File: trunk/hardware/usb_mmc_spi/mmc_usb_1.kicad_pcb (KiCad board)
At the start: 2 copper layers, 47.6 x 27.3 mm, 25 parts, among them J301 MINI-USB-5P-3400020P1, K301 CONN_3, P301 CONN_5X2, P302 MICRO-SDCARD-CONNECTOR-330006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, P303 CONN_10X2, P304 CONN_10X2, P305 CONN_1, P306 CONN_1, U301 FT232RL

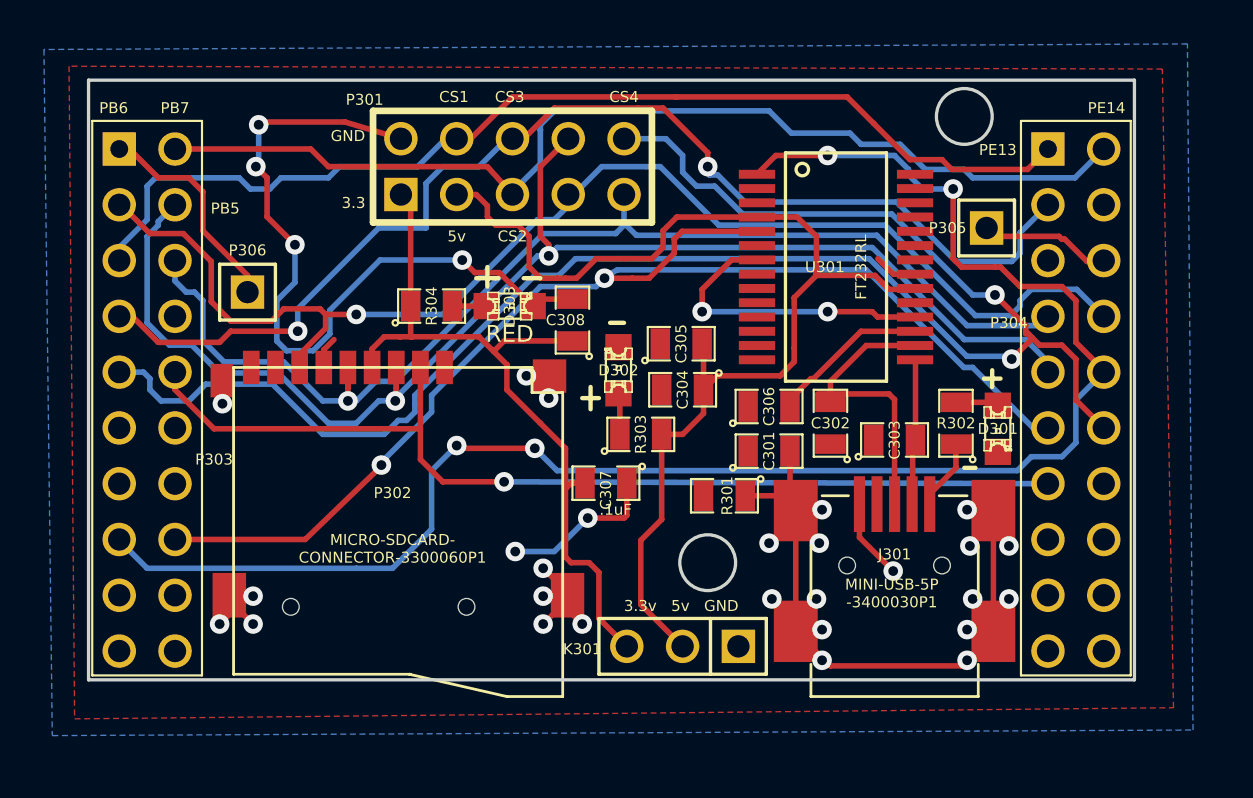
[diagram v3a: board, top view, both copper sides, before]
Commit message: better naming
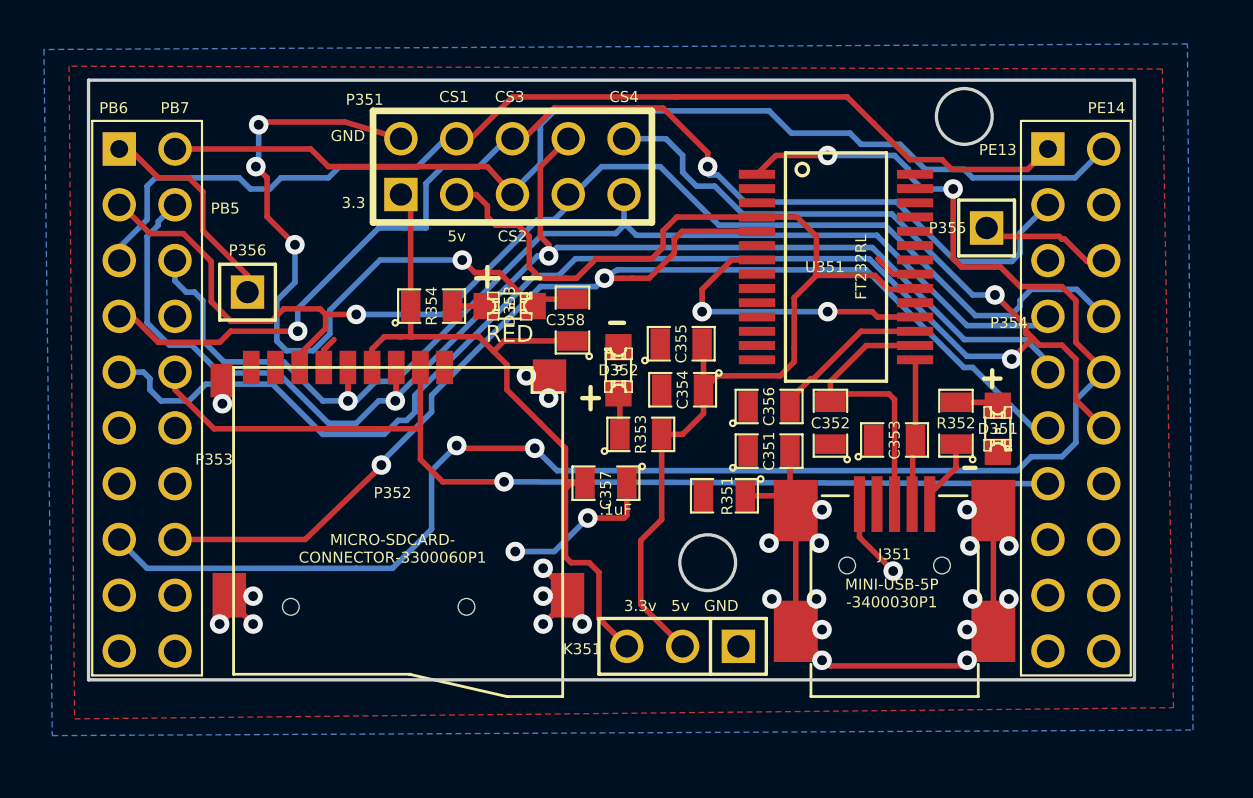
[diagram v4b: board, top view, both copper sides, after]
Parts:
- renumbered C301 to C351, C302 to C352, C303 to C353, C304 to C354, C305 to C355, C306 to C356, C307 to C357, C308 to C358, D301 to D351, D302 to D352, D303 to D353, J301 to J351, K301 to K351, P301 to P351, P302 to P352, P303 to P353, P304 to P354, P305 to P355, P306 to P356, R301 to R351, R302 to R352, R303 to R353, R304 to R354, U301 to U351
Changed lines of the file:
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@@
     (tags "MICRO SD MEMORY CARD MMC")
     (attr smd)
-    (fp_text reference P302 (at -1.778 0.254 360) (layer F.SilkS)
+    (fp_text reference P352 (at -1.778 0.254 360) (layer F.SilkS)
       (effects (font (size 0.50038 0.50038) (thickness 0.1016)))
     )
@@
       (layers F.Cu F.Paste F.Mask)
     )
-    (pad G301 smd rect (at -6.893 8.032 270) (size 1.524 1.016)
+    (pad G351 smd rect (at -6.893 8.032 270) (size 1.524 1.016)
       (layers F.Cu F.Paste F.Mask)
       (net 13 GND)
@@
     (at 207.391 168.656)
     (attr smd)
-    (fp_text reference C301 (at 0 0 90) (layer F.SilkS)
+    (fp_text reference C351 (at 0 0 90) (layer F.SilkS)
       (effects (font (size 0.50038 0.50038) (thickness 0.1016)))
     )
@@
     (at 210.185 167.386 90)
     (attr smd)
-    (fp_text reference C302 (at 0 0 180) (layer F.SilkS)
+    (fp_text reference C352 (at 0 0 180) (layer F.SilkS)
       (effects (font (size 0.50038 0.50038) (thickness 0.1016)))
     )
@@
     (at 213.106 168.148)
     (attr smd)
-    (fp_text reference C303 (at 0 0 90) (layer F.SilkS)
+    (fp_text reference C353 (at 0 0 90) (layer F.SilkS)
       (effects (font (size 0.50038 0.50038) (thickness 0.1016)))
     )
@@
     (at 203.454 165.862 180)
     (attr smd)
-    (fp_text reference C304 (at 0 0 270) (layer F.SilkS)
+    (fp_text reference C354 (at 0 0 270) (layer F.SilkS)
       (effects (font (size 0.50038 0.50038) (thickness 0.1016)))
     )
@@
     (at 203.3905 163.7665)
     (attr smd)
-    (fp_text reference C305 (at 0 0 90) (layer F.SilkS)
+    (fp_text reference C355 (at 0 0 90) (layer F.SilkS)
       (effects (font (size 0.50038 0.50038) (thickness 0.1016)))
     )
@@
     (at 207.391 166.624)
     (attr smd)
-    (fp_text reference C306 (at 0 0 90) (layer F.SilkS)
+    (fp_text reference C356 (at 0 0 90) (layer F.SilkS)
       (effects (font (size 0.50038 0.50038) (thickness 0.1016)))
     )
@@
     (tags "LED 0805 SMD")
     (attr smd)
-    (fp_text reference D301 (at 0 0 360) (layer F.SilkS)
+    (fp_text reference D351 (at 0 0 360) (layer F.SilkS)
       (effects (font (size 0.50038 0.50038) (thickness 0.1016)))
     )
@@
     (tags "LED 0805 SMD")
     (attr smd)
-    (fp_text reference D302 (at 0 0 180) (layer F.SilkS)
+    (fp_text reference D352 (at 0 0 180) (layer F.SilkS)
       (effects (font (size 0.50038 0.50038) (thickness 0.1016)))
     )
@@
     (at 205.359 170.688 180)
     (attr smd)
-    (fp_text reference R301 (at -0.127 0 270) (layer F.SilkS)
+    (fp_text reference R351 (at -0.127 0 270) (layer F.SilkS)
       (effects (font (size 0.50038 0.50038) (thickness 0.1016)))
     )
@@
     (at 215.9 167.386 90)
     (attr smd)
-    (fp_text reference R302 (at 0 0 180) (layer F.SilkS)
+    (fp_text reference R352 (at 0 0 180) (layer F.SilkS)
       (effects (font (size 0.50038 0.50038) (thickness 0.1016)))
     )
@@
     (at 201.549 167.894)
     (attr smd)
-    (fp_text reference R303 (at 0 0 90) (layer F.SilkS)
+    (fp_text reference R353 (at 0 0 90) (layer F.SilkS)
       (effects (font (size 0.50038 0.50038) (thickness 0.1016)))
     )
@@
     (at 210.439 160.274 270)
     (descr SSOP-16)
-    (fp_text reference U301 (at 0 0.508 360) (layer F.SilkS)
+    (fp_text reference U351 (at 0 0.508 360) (layer F.SilkS)
       (effects (font (size 0.50038 0.50038) (thickness 0.1016)))
     )
@@
     (tags "LED 0805 SMD")
     (attr smd)
-    (fp_text reference D303 (at 0 0 90) (layer F.SilkS)
+    (fp_text reference D353 (at 0 0 90) (layer F.SilkS)
       (effects (font (size 0.50038 0.50038) (thickness 0.1016)))
     )
@@
     (at 192.024 162.052)
     (attr smd)
-    (fp_text reference R304 (at 0 0 90) (layer F.SilkS)
+    (fp_text reference R354 (at 0 0 90) (layer F.SilkS)
       (effects (font (size 0.50038 0.50038) (thickness 0.1016)))
     )
@@
     (descr "Connecter 3 pins")
     (tags "PIN 3")
-    (fp_text reference K301 (at 4.572 -0.127 180) (layer F.SilkS)
+    (fp_text reference K351 (at 4.572 -0.127 180) (layer F.SilkS)
       (effects (font (size 0.50038 0.50038) (thickness 0.1016)))
     )
@@
   (module PIN_ARRAY_10X2 (layer F.Cu)
     (at 179.07 166.37 270)
-    (fp_text reference P303 (at 2.667 -3.048 360) (layer F.SilkS)
+    (fp_text reference P353 (at 2.667 -3.048 360) (layer F.SilkS)
       (effects (font (size 0.50038 0.50038) (thickness 0.1016)))
     )
@@
   (module PIN_ARRAY_10X2 (layer F.Cu)
     (at 221.361 166.37 270)
-    (fp_text reference P304 (at -3.556 3.048 360) (layer F.SilkS)
+    (fp_text reference P354 (at -3.556 3.048 360) (layer F.SilkS)
       (effects (font (size 0.50038 0.50038) (thickness 0.1016)))
     )
@@
     (tags "USB MINI 5 SMD-1")
     (attr smd)
-    (fp_text reference J301 (at 0 -1.905) (layer F.SilkS)
+    (fp_text reference J351 (at 0 -1.905) (layer F.SilkS)
       (effects (font (size 0.50038 0.50038) (thickness 0.1016)))
     )
@@
     (descr "1 pin")
     (tags "CONN DEV")
-    (fp_text reference P305 (at -1.778 0) (layer F.SilkS)
+    (fp_text reference P355 (at -1.778 0) (layer F.SilkS)
       (effects (font (size 0.50038 0.50038) (thickness 0.1016)))
     )
@@
     (descr "Double rangee de contacts 2 x 5 pins")
     (tags CONN)
-    (fp_text reference P301 (at -6.731 -3.048) (layer F.SilkS)
+    (fp_text reference P351 (at -6.731 -3.048) (layer F.SilkS)
       (effects (font (size 0.50038 0.50038) (thickness 0.1016)))
     )
@@
     (descr "1 pin")
     (tags "CONN DEV")
-    (fp_text reference P306 (at 0 -1.905) (layer F.SilkS)
+    (fp_text reference P356 (at 0 -1.905) (layer F.SilkS)
       (effects (font (size 0.50038 0.50038) (thickness 0.1016)))
     )
@@
     (at 199.9615 170.1165 180)
     (attr smd)
-    (fp_text reference C307 (at 0 -0.3175 270) (layer F.SilkS)
+    (fp_text reference C357 (at 0 -0.3175 270) (layer F.SilkS)
       (effects (font (size 0.50038 0.50038) (thickness 0.10922)))
     )
@@
     (at 198.4375 162.687 90)
     (attr smd)
-    (fp_text reference C308 (at 0 -0.3175 180) (layer F.SilkS)
+    (fp_text reference C358 (at 0 -0.3175 180) (layer F.SilkS)
       (effects (font (size 0.50038 0.50038) (thickness 0.10922)))
     )

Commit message: CAN_TX net
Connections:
- net N-0000033 renamed /CAN_TX

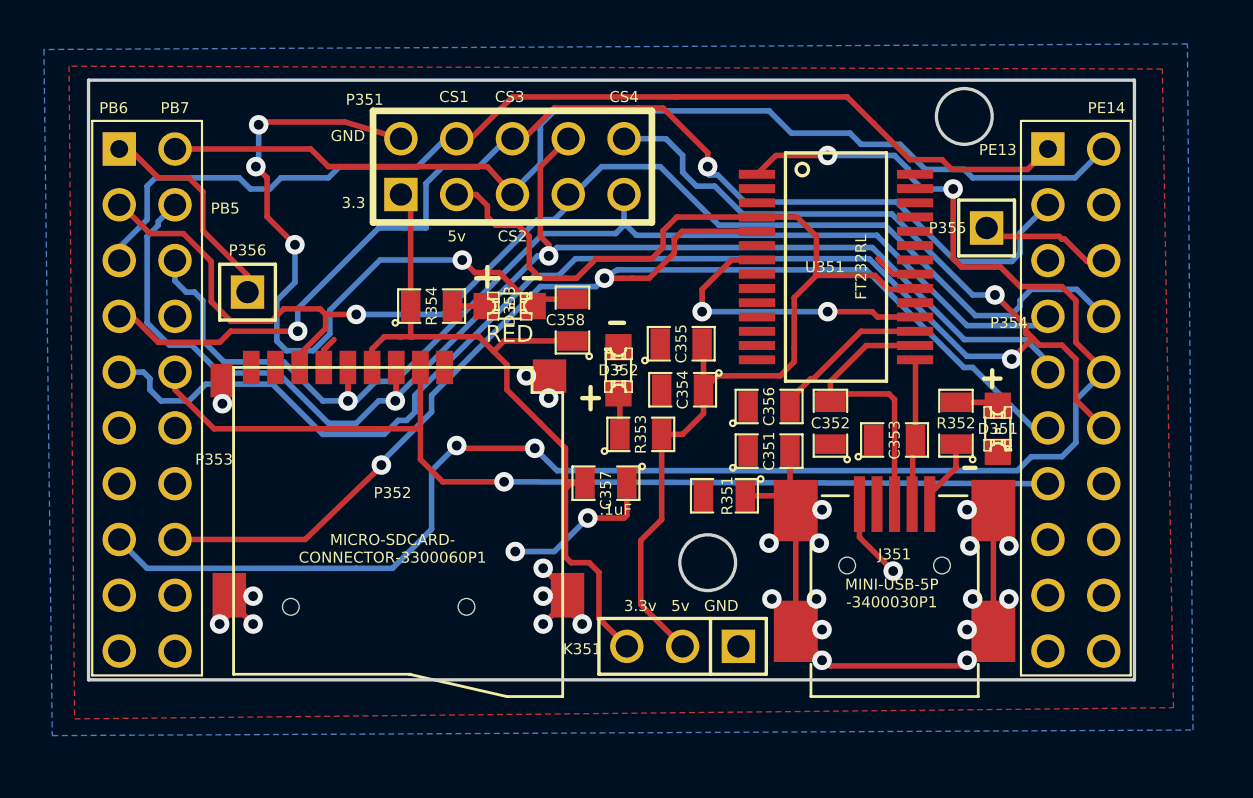
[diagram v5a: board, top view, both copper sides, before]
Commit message: some track improvements
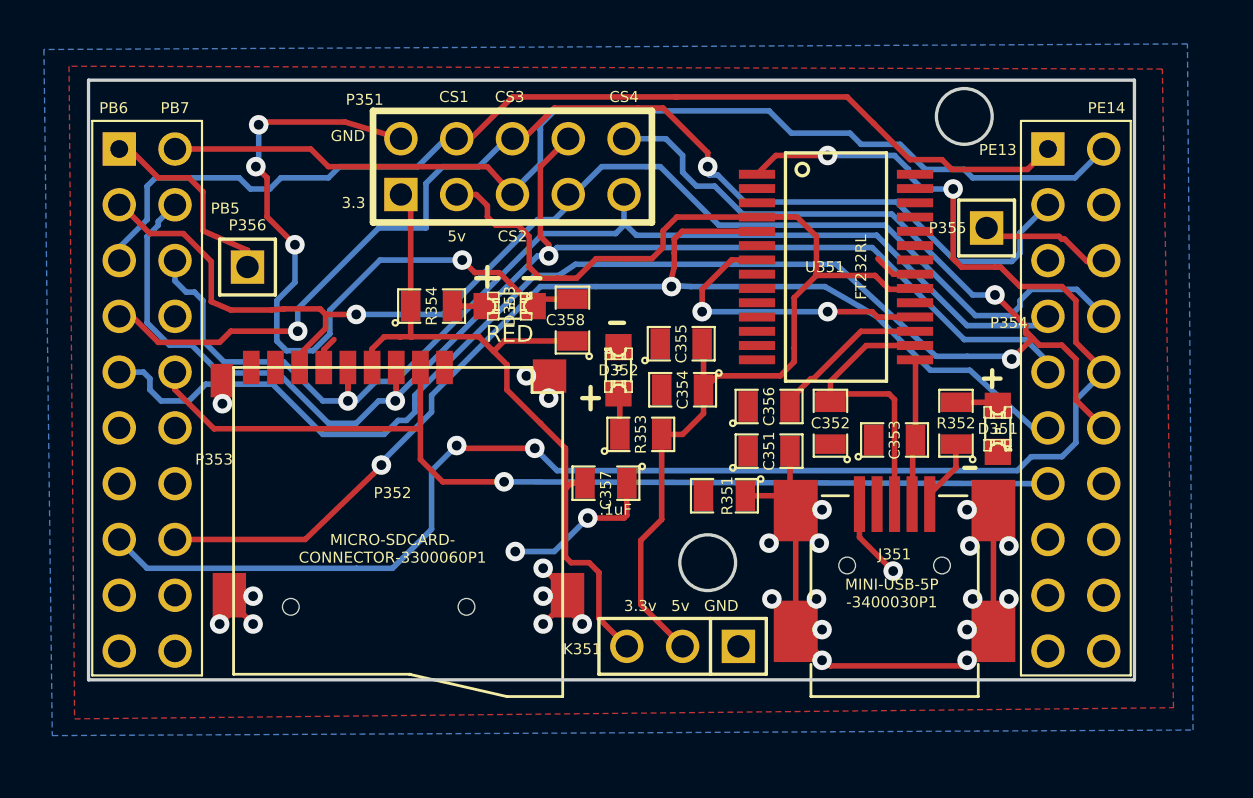
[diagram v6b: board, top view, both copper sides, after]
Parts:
- moved P356 1.14 mm to (183.6, 160.3)
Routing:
- net /USART_RX: track 56.5 -> 53.6 mm
- net /CAN_TX: track 10.0 -> 9.37 mm
- net /SPI_MISO: track 58.4 -> 57.9 mm
